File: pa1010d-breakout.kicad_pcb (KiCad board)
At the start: 2 copper layers, 21 x 23.5 mm, 4 parts, among them J1 Conn_01x08_Male, U1 PA1010D

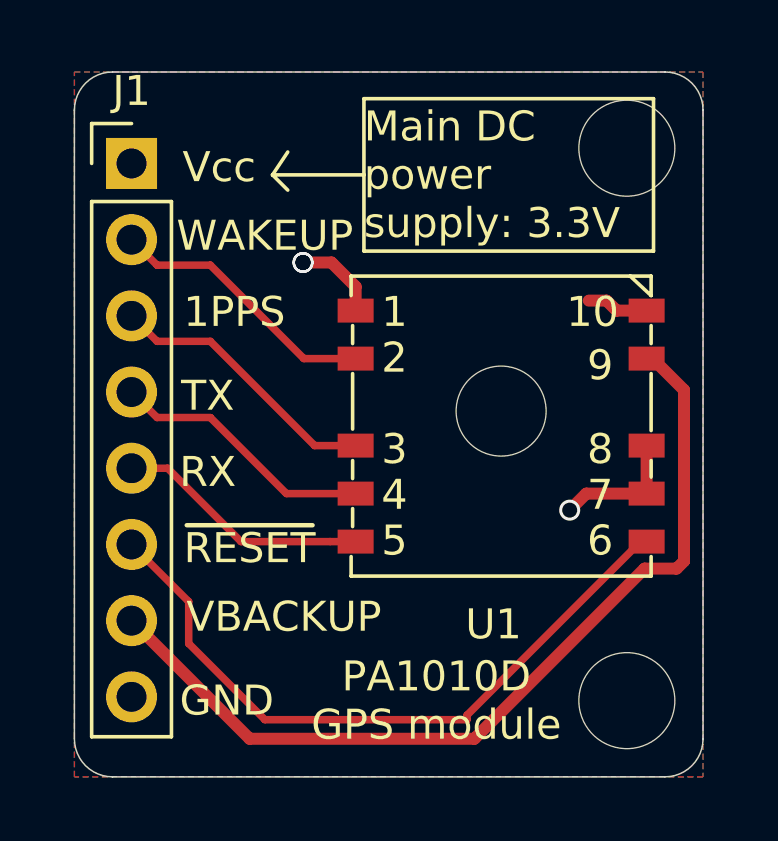
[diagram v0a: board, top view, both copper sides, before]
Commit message: refactor: update PCB layout to make it smaller and add more infor in silkscreen
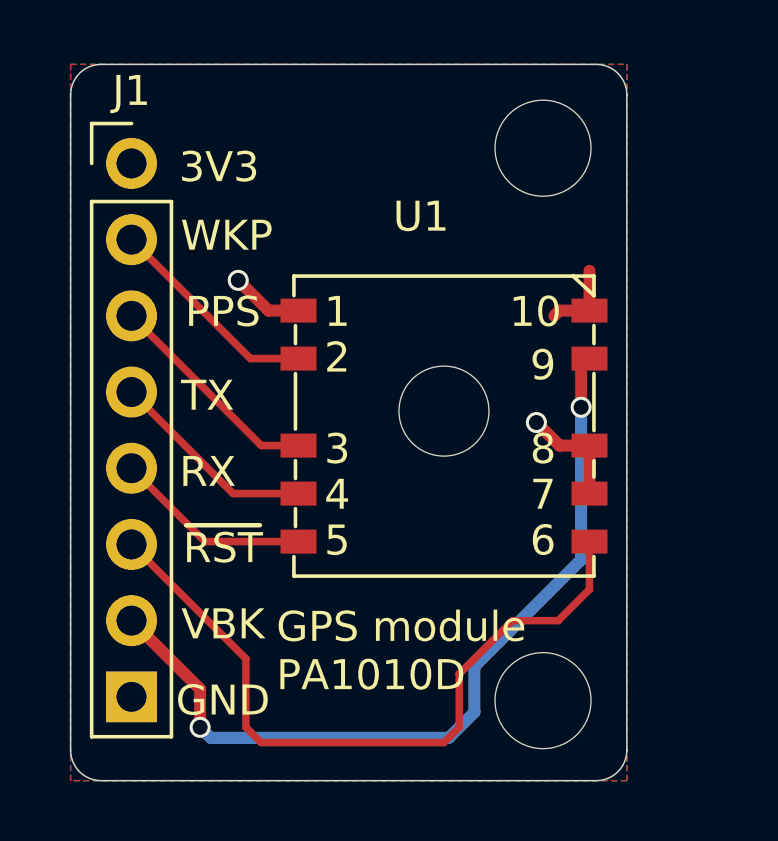
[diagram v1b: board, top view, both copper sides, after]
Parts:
- added REF**: OSHW-Logo2_7.3x6mm_SilkScreen, Symbol:OSHW-Logo2_7.3x6mm_SilkScreen, B.Cu at (94.7, 72.6)
- moved REF** 2.79 mm to (100.1, 72.4)
- moved REF** 2.79 mm to (100.1, 90.8)
- moved U1 1.91 mm to (96.8, 81.2)
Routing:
- net /VBACKUP: track 29.9 -> 27.5 mm, vias 0 -> 2
- net /WAKEUP: track 9.11 -> 7.21 mm
- net /RX: track 8.48 -> 6.58 mm
- net /TX: track 8.87 -> 6.97 mm
- net /1PPS: track 9.26 -> 7.36 mm
- net GND: track 7.48 -> 6.11 mm, vias 3 -> 2
- net /NRESET: track 23.0 -> 24.1 mm
- net +3V3: track 2.07 -> 2.57 mm
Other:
- board size 21 x 23.5 mm -> 18.5 x 23.9 mm
- board text added: "3V3"
- board text added: "GPS module PA1010D"
- board text added: "PA1010D Breakout"
- board text added: "PPS"
- board text added: "V1.0 Nov 2019"
- board text added: "VBK"
- board text added: "WKP"
- board text added: "bit.ly/pa1010d"
- board text added: "~RST"
- board text removed: "1PPS"
- board text removed: "Main DC power supply: 3.3V"
- board text removed: "PA1010D GPS module"
- board text removed: "VBACKUP"
- board text removed: "Vcc"
- board text removed: "WAKEUP"
- board text removed: "~RESET"

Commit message: refactor: change to 1mm grid for edge cuts
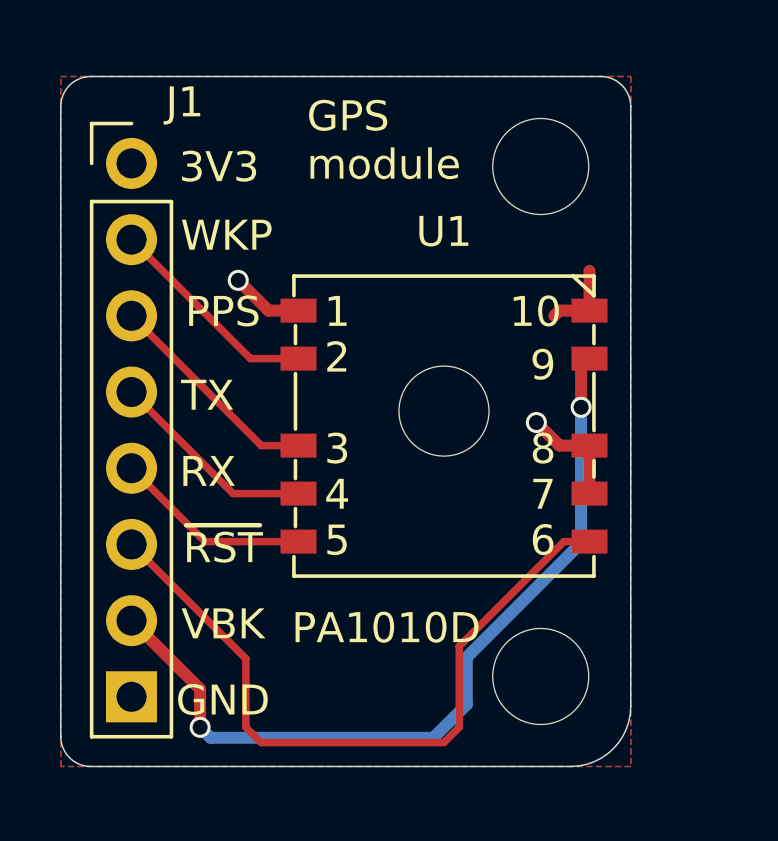
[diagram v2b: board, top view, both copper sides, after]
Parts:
- moved REF** 0.81 mm to (100.0, 90.0)
- moved REF** 0.61 mm to (100.0, 73.0)
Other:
- board size 18.5 x 23.9 mm -> 19 x 23 mm
- board text added: "GPS module"
- board text added: "PA1010D"
- board text removed: "GPS module PA1010D"
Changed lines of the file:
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@@
-(kicad_pcb (version 20171130) (host pcbnew "(5.1.0-0)")
+(kicad_pcb (version 20171130) (host pcbnew "(5.1.5-0-10_14)")
   (general
     (thickness 1.6)
-    (drawings 42)
-    (tracks 40)
+    (drawings 43)
+    (tracks 38)
     (zones 0)
     (modules 5)
@@
   (layers
     (0 F.Cu signal)
-    (31 B.Cu signal hide)
+    (31 B.Cu signal)
     (32 B.Adhes user hide)
     (33 F.Adhes user hide)
@@
     (47 F.CrtYd user)
     (48 B.Fab user hide)
-    (49 F.Fab user)
+    (49 F.Fab user hide)
   )
   (setup
@@
     (solder_mask_min_width 0.25)
     (aux_axis_origin 0 0)
-    (visible_elements FFFFFF7F)
+    (visible_elements FFFFEF7F)
     (pcbplotparams
       (layerselection 0x010fc_ffffffff)
@@
   (module CDTop_PA1010D:CDTop_MT3333_PA1010D (layer F.Cu)
     (at 96.774 81.153)
-    (fp_text reference U1 (at -0.762 -6.477) (layer F.SilkS)
+    (fp_text reference U1 (at 0 -5.969) (layer F.SilkS)
       (effects (font (size 1 1) (thickness 0.15)))
     )
@@
   )
   (module MountingHole:MountingHole_3.2mm_M3 (layer F.Cu)
-    (at 100.076 72.39)
+    (at 100 73)
     (descr "Mounting Hole 3.2mm, no annular, M3")
     (tags "mounting hole 3.2mm no annular m3")
@@
   )
   (module MountingHole:MountingHole_3.2mm_M3 (layer F.Cu)
-    (at 100.076 90.805)
+    (at 100 90)
     (descr "Mounting Hole 3.2mm, no annular, M3")
     (tags "mounting hole 3.2mm no annular m3")
@@
     (descr "Through hole straight pin header, 1x08, 2.54mm pitch, single row")
     (tags "Through hole pin header THT 1x08 2.54mm single row")
-    (fp_text reference J1 (at 0 -2.413) (layer F.SilkS)
+    (fp_text reference J1 (at 1.778 -2.032) (layer F.SilkS)
       (effects (font (size 1 1) (thickness 0.15)))
     )
@@
     )
   )
+  (dimension 23 (width 0.15) (layer Dwgs.User)
+    (gr_text "23.000 mm" (at 105.3 81.5 90) (layer Dwgs.User)
+      (effects (font (size 1 1) (thickness 0.15)))
+    )
+    (feature1 (pts (xy 101 70) (xy 104.586421 70)))
+    (feature2 (pts (xy 101 93) (xy 104.586421 93)))
+    (crossbar (pts (xy 104 93) (xy 104 70)))
+    (arrow1a (pts (xy 104 70) (xy 104.586421 71.126504)))
+    (arrow1b (pts (xy 104 70) (xy 103.413579 71.126504)))
+    (arrow2a (pts (xy 104 93) (xy 104.586421 91.873496)))
+    (arrow2b (pts (xy 104 93) (xy 103.413579 91.873496)))
+  )
+  (dimension 19 (width 0.15) (layer Dwgs.User)
+    (gr_text "19.000 mm" (at 93.5 67.7) (layer Dwgs.User)
+      (effects (font (size 1 1) (thickness 0.15)))
+    )
+    (feature1 (pts (xy 103 71) (xy 103 68.413579)))
+    (feature2 (pts (xy 84 71) (xy 84 68.413579)))
+    (crossbar (pts (xy 84 69) (xy 103 69)))
+    (arrow1a (pts (xy 103 69) (xy 101.873496 69.586421)))
+    (arrow1b (pts (xy 103 69) (xy 101.873496 68.413579)))
+    (arrow2a (pts (xy 84 69) (xy 85.126504 69.586421)))
+    (arrow2b (pts (xy 84 69) (xy 85.126504 68.413579)))
+  )
+  (gr_text PA1010D (at 91.694 88.392) (layer F.SilkS)
+    (effects (font (size 1 1) (thickness 0.15)) (justify left))
+  )
+  (gr_line (start 84 92) (end 84 71) (layer Edge.Cuts) (width 0.05))
+  (gr_line (start 101 93) (end 85 93) (layer Edge.Cuts) (width 0.05))
+  (gr_line (start 103 71) (end 103 91) (layer Edge.Cuts) (width 0.05))
+  (gr_line (start 85 70) (end 102 70) (layer Edge.Cuts) (width 0.05))
+  (gr_arc (start 101 91) (end 101 93) (angle -90) (layer Edge.Cuts) (width 0.05))
+  (gr_arc (start 85 92) (end 84 92) (angle -90) (layer Edge.Cuts) (width 0.05))
+  (gr_arc (start 85 71) (end 85 70) (angle -90) (layer Edge.Cuts) (width 0.05))
+  (gr_arc (start 102 71) (end 103 71) (angle -90) (layer Edge.Cuts) (width 0.05))
   (gr_line (start 90.932 78.74) (end 91.186 78.74) (layer B.SilkS) (width 0.12))
   (gr_line (start 90.932 75.692) (end 90.932 78.74) (layer B.SilkS) (width 0.12))
@@
     (effects (font (size 1 1) (thickness 0.15)) (justify mirror))
   )
-  (dimension 23.876 (width 0.15) (layer Dwgs.User)
-    (gr_text "23.876 mm" (at 105.694 81.534 90) (layer Dwgs.User)
-      (effects (font (size 1 1) (thickness 0.15)))
-    )
-    (feature1 (pts (xy 101.854 69.596) (xy 104.980421 69.596)))
-    (feature2 (pts (xy 101.854 93.472) (xy 104.980421 93.472)))
-    (crossbar (pts (xy 104.394 93.472) (xy 104.394 69.596)))
-    (arrow1a (pts (xy 104.394 69.596) (xy 104.980421 70.722504)))
-    (arrow1b (pts (xy 104.394 69.596) (xy 103.807579 70.722504)))
-    (arrow2a (pts (xy 104.394 93.472) (xy 104.980421 92.345496)))
-    (arrow2b (pts (xy 104.394 93.472) (xy 103.807579 92.345496)))
-  )
-  (dimension 18.542 (width 0.15) (layer Dwgs.User)
-    (gr_text "18.542 mm" (at 93.599 67.026) (layer Dwgs.User)
-      (effects (font (size 1 1) (thickness 0.15)))
-    )
-    (feature1 (pts (xy 102.87 70.866) (xy 102.87 67.739579)))
-    (feature2 (pts (xy 84.328 70.866) (xy 84.328 67.739579)))
-    (crossbar (pts (xy 84.328 68.326) (xy 102.87 68.326)))
-    (arrow1a (pts (xy 102.87 68.326) (xy 101.743496 68.912421)))
-    (arrow1b (pts (xy 102.87 68.326) (xy 101.743496 67.739579)))
-    (arrow2a (pts (xy 84.328 68.326) (xy 85.454504 68.912421)))
-    (arrow2b (pts (xy 84.328 68.326) (xy 85.454504 67.739579)))
-  )
-  (gr_line (start 84.328 70.612) (end 84.328 92.456) (layer Edge.Cuts) (width 0.05))
-  (gr_line (start 101.854 69.596) (end 85.344 69.596) (layer Edge.Cuts) (width 0.05))
-  (gr_line (start 102.87 92.456) (end 102.87 70.612) (layer Edge.Cuts) (width 0.05))
-  (gr_line (start 85.344 93.472) (end 101.854 93.472) (layer Edge.Cuts) (width 0.05))
-  (gr_arc (start 85.344 92.456) (end 84.328 92.456) (angle -90) (layer Edge.Cuts) (width 0.05))
-  (gr_arc (start 101.854 92.456) (end 101.854 93.472) (angle -90) (layer Edge.Cuts) (width 0.05))
-  (gr_arc (start 101.854 70.612) (end 102.87 70.612) (angle -90) (layer Edge.Cuts) (width 0.05))
-  (gr_arc (start 85.344 70.612) (end 85.344 69.596) (angle -90) (layer Edge.Cuts) (width 0.05))
   (gr_text ~RST (at 89.408 85.725) (layer F.SilkS)
     (effects (font (size 1 1) (thickness 0.15)))
@@
     (effects (font (size 1 1) (thickness 0.15)))
   )
-  (gr_text "GPS module\nPA1010D\n" (at 91.186 89.154) (layer F.SilkS)
+  (gr_text "GPS \nmodule\n" (at 92.202 72.136) (layer F.SilkS)
     (effects (font (size 1 1) (thickness 0.15)) (justify left))
   )
@@
   (segment (start 88.646 90.424) (end 88.646 91.694) (width 0.4) (layer F.Cu) (net 3))
   (via (at 88.646 91.694) (size 0.7) (drill 0.5) (layers F.Cu B.Cu) (net 3))
-  (segment (start 88.995999 92.043999) (end 96.932001 92.043999) (width 0.4) (layer B.Cu) (net 3))
   (segment (start 88.646 91.694) (end 88.995999 92.043999) (width 0.4) (layer B.Cu) (net 3))
-  (segment (start 96.932001 92.043999) (end 97.79 91.186) (width 0.4) (layer B.Cu) (net 3))
-  (segment (start 97.79 89.662) (end 101.346 86.106) (width 0.4) (layer B.Cu) (net 3))
-  (segment (start 97.79 91.186) (end 97.79 89.662) (width 0.4) (layer B.Cu) (net 3))
-  (segment (start 101.346 86.106) (end 101.346 81.026) (width 0.4) (layer B.Cu) (net 3))
   (via (at 101.346 81.026) (size 0.7) (drill 0.5) (layers F.Cu B.Cu) (net 3))
   (segment (start 101.346 79.681) (end 101.624 79.403) (width 0.4) (layer F.Cu) (net 3))
   (segment (start 101.346 81.026) (end 101.346 79.681) (width 0.4) (layer F.Cu) (net 3))
-  (segment (start 101.624 87.098) (end 101.624 85.503) (width 0.25) (layer F.Cu) (net 4))
-  (segment (start 100.584 88.138) (end 101.624 87.098) (width 0.25) (layer F.Cu) (net 4))
-  (segment (start 99.06 88.138) (end 100.584 88.138) (width 0.25) (layer F.Cu) (net 4))
-  (segment (start 97.282 89.916) (end 99.06 88.138) (width 0.25) (layer F.Cu) (net 4))
-  (segment (start 97.282 91.694) (end 97.282 89.916) (width 0.25) (layer F.Cu) (net 4))
+  (segment (start 88.995999 92.043999) (end 96.424001 92.043999) (width 0.4) (layer B.Cu) (net 3))
+  (segment (start 96.424001 92.043999) (end 97.536 90.932) (width 0.4) (layer B.Cu) (net 3))
+  (segment (start 97.536 89.355998) (end 101.346 85.545998) (width 0.4) (layer B.Cu) (net 3))
+  (segment (start 97.536 90.932) (end 97.536 89.355998) (width 0.4) (layer B.Cu) (net 3))
+  (segment (start 101.346 85.545998) (end 101.346 81.026) (width 0.4) (layer B.Cu) (net 3))
+  (segment (start 97.282 88.995) (end 100.774 85.503) (width 0.25) (layer F.Cu) (net 4))
+  (segment (start 97.282 91.694) (end 97.282 88.995) (width 0.25) (layer F.Cu) (net 4))
+  (segment (start 100.774 85.503) (end 101.624 85.503) (width 0.25) (layer F.Cu) (net 4))
+  (segment (start 96.774 92.202) (end 97.282 91.694) (width 0.25) (layer F.Cu) (net 4))
   (segment (start 90.678 92.202) (end 96.774 92.202) (width 0.25) (layer F.Cu) (net 4))
   (segment (start 90.17 91.694) (end 90.678 92.202) (width 0.25) (layer F.Cu) (net 4))
-  (segment (start 96.774 92.202) (end 97.282 91.694) (width 0.25) (layer F.Cu) (net 4))
   (segment (start 90.17 89.408) (end 90.17 91.694) (width 0.25) (layer F.Cu) (net 4))
   (segment (start 86.36 85.598) (end 90.17 89.408) (width 0.25) (layer F.Cu) (net 4))
@@
     (polygon
       (pts
-        (xy 84.328 69.596) (xy 102.87 69.596) (xy 102.87 93.472) (xy 84.328 93.472)
+        (xy 103 93) (xy 84 93) (xy 84 70) (xy 103 70)
       )
     )
@@
     (polygon
       (pts
-        (xy 84.328 69.596) (xy 102.87 69.596) (xy 102.87 93.472) (xy 84.328 93.472)
+        (xy 103 93) (xy 84 93) (xy 84 70) (xy 103 70)
       )
     )
